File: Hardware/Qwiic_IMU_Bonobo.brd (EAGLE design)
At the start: 30.5 x 25.4 mm, 33 parts, among them J2 SMD, J3 PTH, J4 SMD, J6 SPI, U2 BNO080

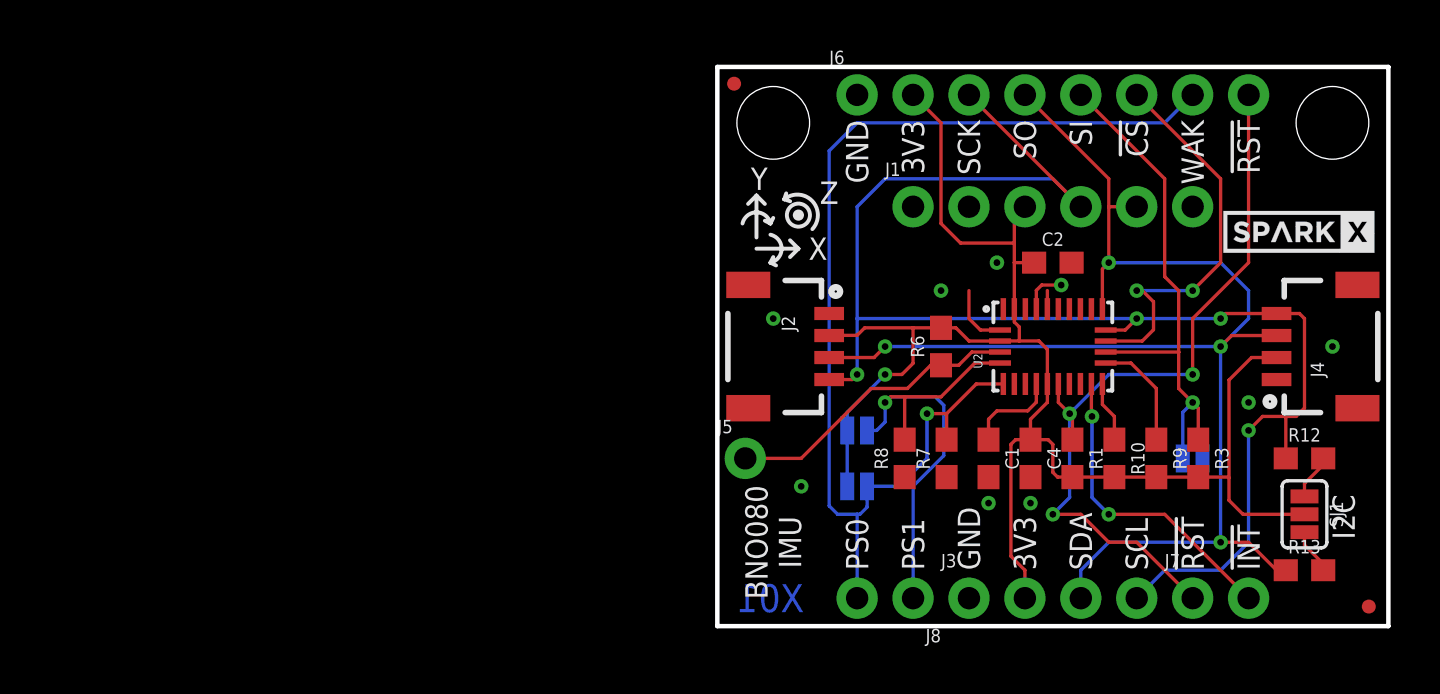
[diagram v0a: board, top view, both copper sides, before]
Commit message: Adding 32kHz xtal. Fixing UART silk.
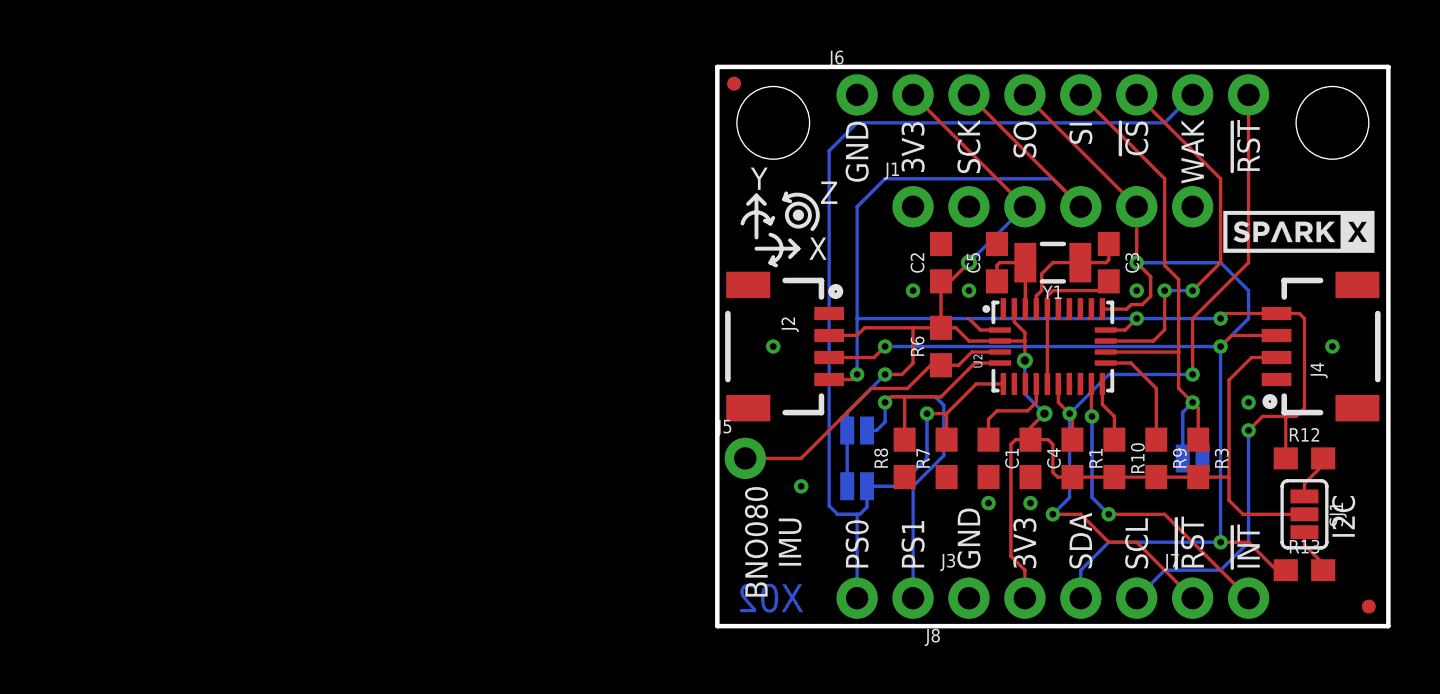
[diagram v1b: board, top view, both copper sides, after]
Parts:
- added C3, C5: 22pF, SparkFun-Capacitors:0603
- added Y1: 32.768kHz, SparkFun-Clocks:CRYSTAL-SMD-3.2X1.5MM
- moved C2 5.08 mm to (10.2, 16.5), turned to 90 degrees
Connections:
- new net N$1: C5.1, U2.27, Y1.P$2
- new net N$2: C3.1, U2.26, Y1.P$1
- net 3.3V: no longer U2.10
- net GND: now also C3.2, C5.2, U2.10; no longer U2.26
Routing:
- net N$2: track 0.00 -> 5.74 mm
- net N$1: track 0.00 -> 4.18 mm
- net GND: track 5.82 -> 8.68 mm
- net 3.3V: track 71.6 -> 69.9 mm, vias 1 -> 4
- net !CS: track 18.2 -> 16.9 mm
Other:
- board text added: "X02"
- board text removed: "3V#"
- board text removed: "X01"

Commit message: Label update. PWR LED added. Logo change.
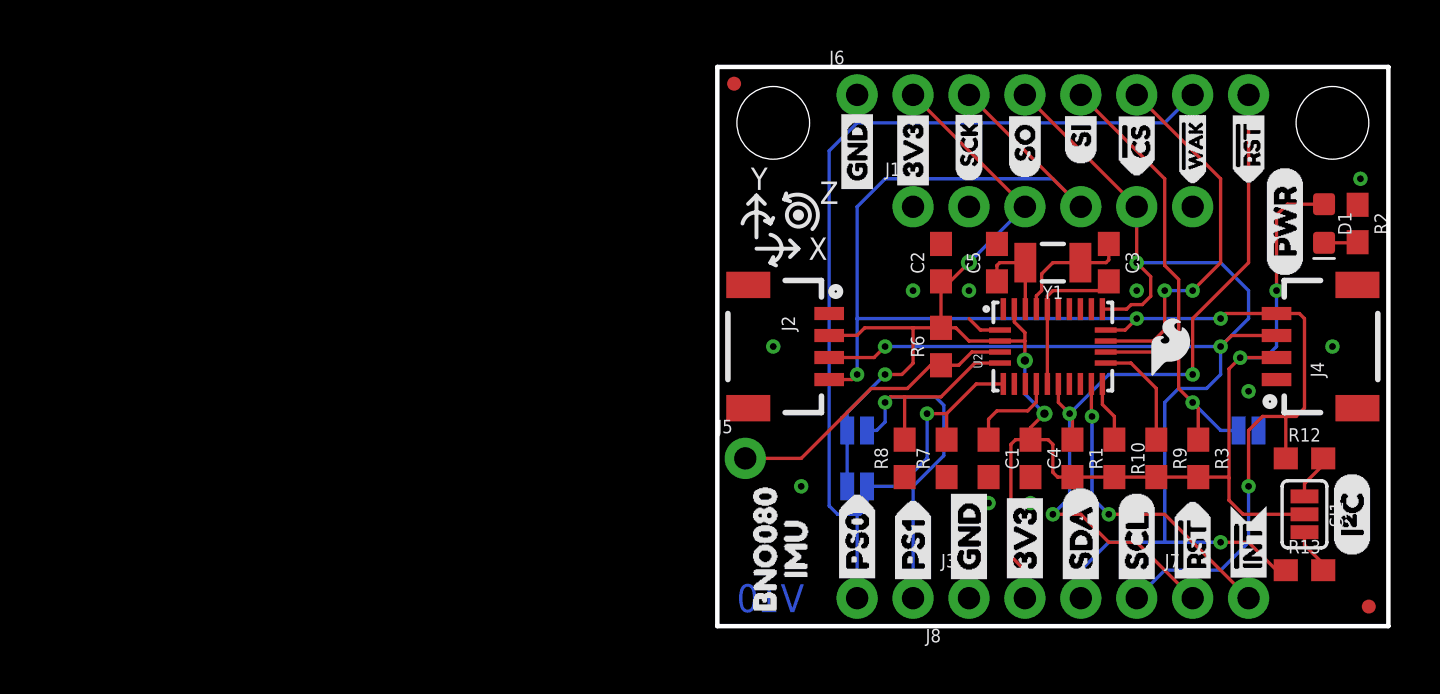
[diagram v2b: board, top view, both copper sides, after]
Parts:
- added D1: RED, SparkFun-LED:LED-0603
- added LOGO4: SFE_LOGO_FLAME.1_INCH, SparkFun-Aesthetics:SFE_LOGO_FLAME_.1
- added LOGO5: SFE_LOGO_NAME_FLAME.1_INCH, SparkFun-Aesthetics:SFE_LOGO_NAME_FLAME_.1
- added R2: 1k, SparkFun-Resistors:0603
- added U$10, U$9: (no value), Labels-0_04:3V3
- added U$11, U$50: (no value), buzzard_labels (4):3V30
- added U$12, U$13: (no value), buzzard_labels (6):SCK0
- added U$14: (no value), buzzard_labels (8):PS03
- added U$15, U$16: (no value), Labels-0_04:GND
- added U$17, U$18: (no value), buzzard_labels (7):SI1
- added U$19, U$20: (no value), buzzard_labels (5):#WAK6
- added U$21: (no value), buzzard_labels (8):3V32
- added U$22: (no value), buzzard_labels (8):RXI1
- added U$23: (no value), Labels-0_04:(I_SUPER2_C)
- added U$25, U$26: (no value), buzzard_labels (2):#INT0
- added U$27, U$28: (no value), buzzard_labels (2):PS14
- added U$29: (no value), buzzard_labels (2):PS05
- added U$3, U$4: (no value), Labels-0_04:#RST>
- added U$30: (no value), buzzard_labels (9):ADR0
- added U$33: (no value), buzzard_labels (2):PS114
- added U$34: (no value), buzzard_labels (2):PS015
- added U$35: (no value), buzzard_labels (8):TXO0
- added U$39: (no value), buzzard_labels (2):UART8
- added U$40: (no value), buzzard_labels (2):GRN10
- added U$41: (no value), buzzard_labels (2):BLK9
- added U$42, U$43: (no value), buzzard_labels (5):GND1
- added U$44: (no value), buzzard_labels (2):BNO080_IMU11
- added U$46: (no value), buzzard_labels (2):BNO08012
- added U$47: (no value), buzzard_labels (2):IMU13
- added U$49, U$51: (no value), buzzard_labels (5):#RST7
- added U$5, U$6: (no value), Labels-0_04:SCL
- added U$52, U$53: (no value), buzzard_labels (6):#CS3
- added U$54, U$55: (no value), buzzard_labels (7):SO0
- added U$7, U$8: (no value), Labels-0_04:SDA
- U$1: value SPARKX-LOGO3 -> (none); device SparkX:SPARKX-SMALL -> Labels-0_04:(PWR)
- U$2: value SPARKX-LOGO3 -> (none); device SparkX:SPARKX-SMALL -> buzzard_labels (11):BOOT2
- moved U$2 27.0 mm to (1.27, 8.00), flipped to the bottom, turned to 90 degrees
- moved U$1 12.0 mm to (25.8, 15.9), flipped to the top, turned to 90 degrees
- moved SJ2 2.84 mm to (24.1, 8.89)
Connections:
- new net N$3: D1.C, R2.2
- net 3.3V: now also D1.A
- net GND: now also R2.1
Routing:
- net 3.3V: track 69.9 -> 80.4 mm, vias 4 -> 6
- net SDA/MISO/TX: track 63.9 -> 65.7 mm
- net N$3: track 0.00 -> 1.54 mm
- net GND: vias 9 -> 10
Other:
- board text added: "V10"
- board text removed: "!CS"
- board text removed: "!INT"
- board text removed: "!RST"
- board text removed: "3V3"
- board text removed: "BLK"
- board text removed: "BNO080 IMU"
- board text removed: "GND"
- board text removed: "GRN"
- board text removed: "I2C"
- board text removed: "I2C ADR"
- board text removed: "PS0"
- board text removed: "PS1"
- board text removed: "RXI"
- board text removed: "SCK"
- board text removed: "SCL"
- board text removed: "SDA"
- board text removed: "SI"
- board text removed: "SO"
- board text removed: "TXO"
- board text removed: "UART"
- board text removed: "WAK"
- board text removed: "X02"

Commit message: Adding dims.
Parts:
- moved U$2 0.13 mm to (1.27, 8.13)

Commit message: Adding fancy Qwiic logo.
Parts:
- added U$24: (no value), Qwiic#Label#png:QWIIC#LABEL#PNG

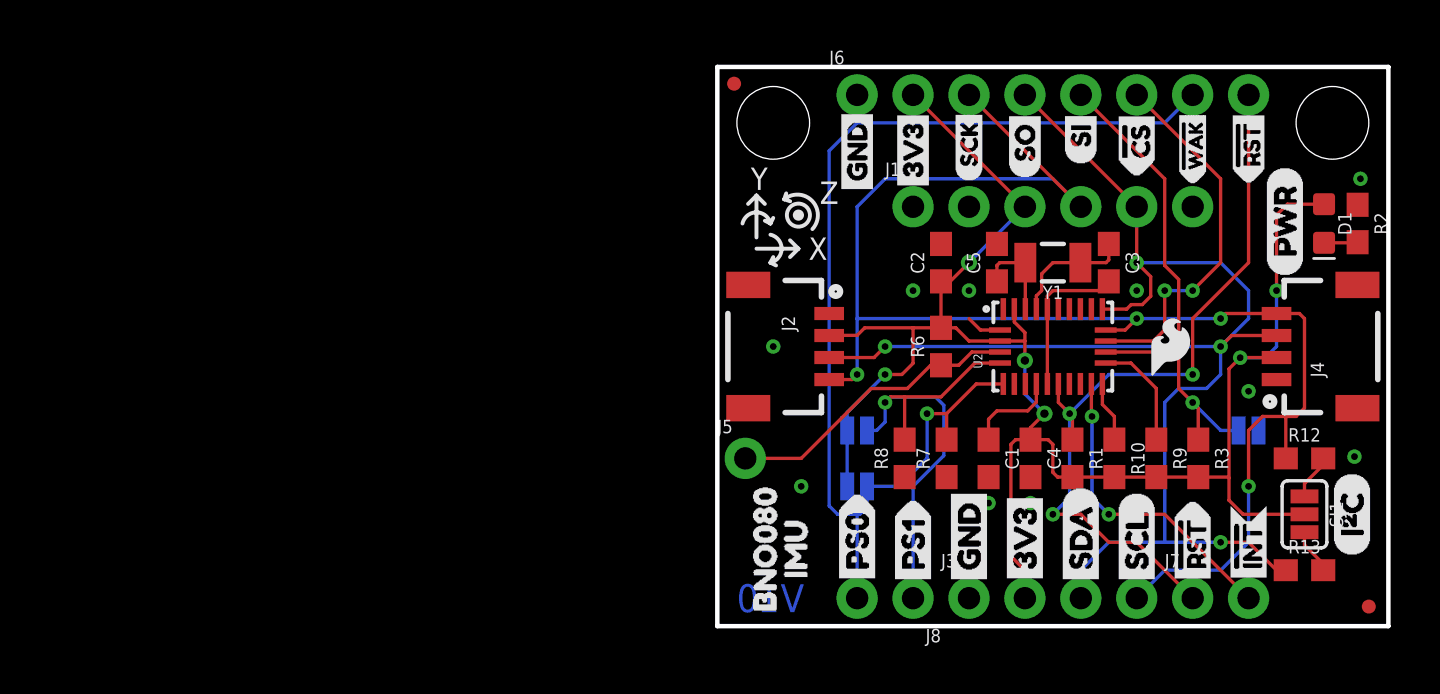
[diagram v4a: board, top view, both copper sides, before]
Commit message: Changing Qwiic logo to w/ word
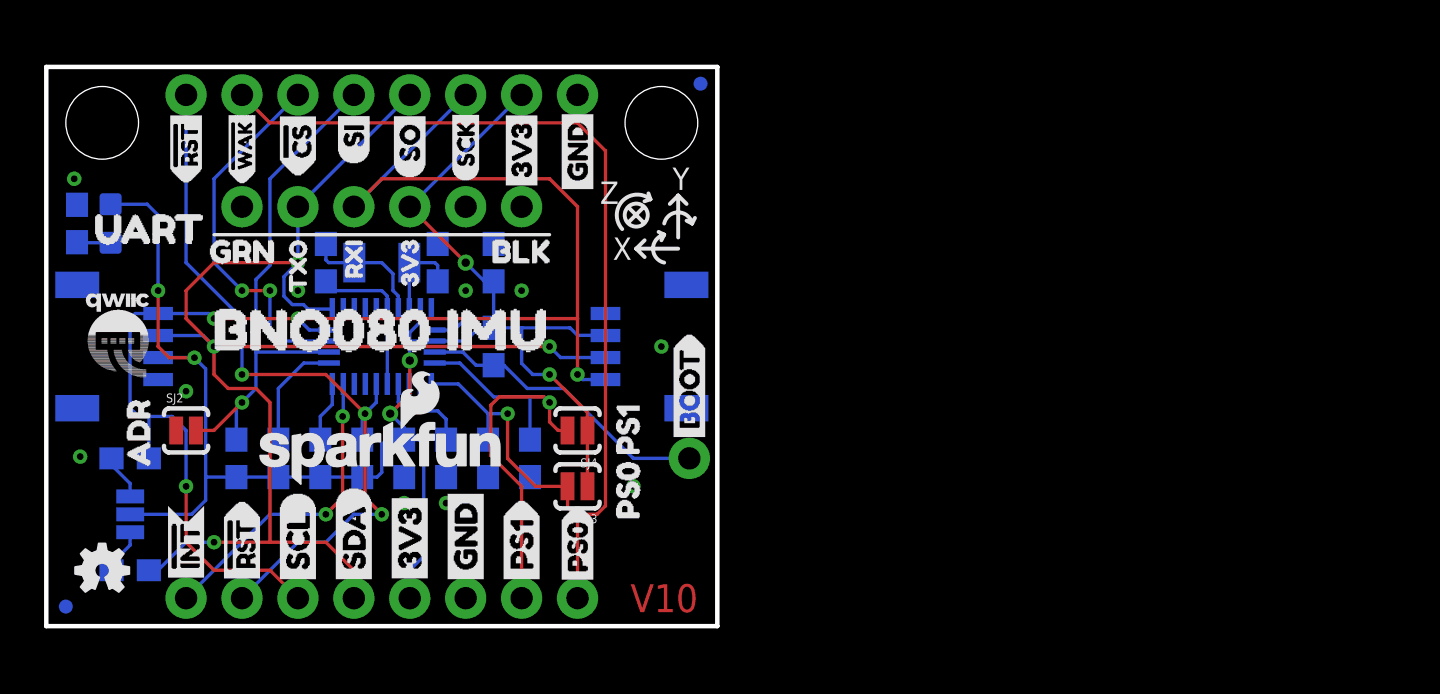
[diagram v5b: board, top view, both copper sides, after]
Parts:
- removed U$24: (no value), Qwiic#Label#png:QWIIC#LABEL#PNG
- added U$59: (no value), Qwiic#Label#Full#M#png (6):QWIIC#LABEL#FULL#M#PNG
- moved JP2 59.2 mm to (-29.6, 0.89), flipped to the bottom
- moved U$39 58.9 mm to (-29.5, 18.0), flipped to the top
- moved R2 58.2 mm to (-29.1, 18.3), flipped to the bottom
- moved U$23 57.7 mm to (-28.8, 3.17), flipped to the bottom
- moved JP4 55.9 mm to (-27.9, 22.9), flipped to the bottom
- moved LOGO1 55.9 mm to (-27.9, 2.54), flipped to the top
- moved D1 55.1 mm to (-27.6, 18.3), flipped to the bottom
- moved R12 53.3 mm to (-26.7, 7.62), flipped to the bottom
- moved R13 53.3 mm to (-26.7, 2.54), flipped to the bottom
- moved SJ1 53.3 mm to (-26.7, 5.08), flipped to the bottom
- moved U$30 52.6 mm to (-26.3, 6.35), flipped to the top
- moved U$1 51.6 mm to (-25.8, 15.9), flipped to the bottom
- moved J4 50.8 mm to (-25.4, 12.7), flipped to the bottom
- moved U$44 49.0 mm to (-24.5, 13.5), flipped to the top
- moved SJ2 48.3 mm to (-24.1, 8.89), flipped to the top
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
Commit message: Adding qwiic logo w/ words
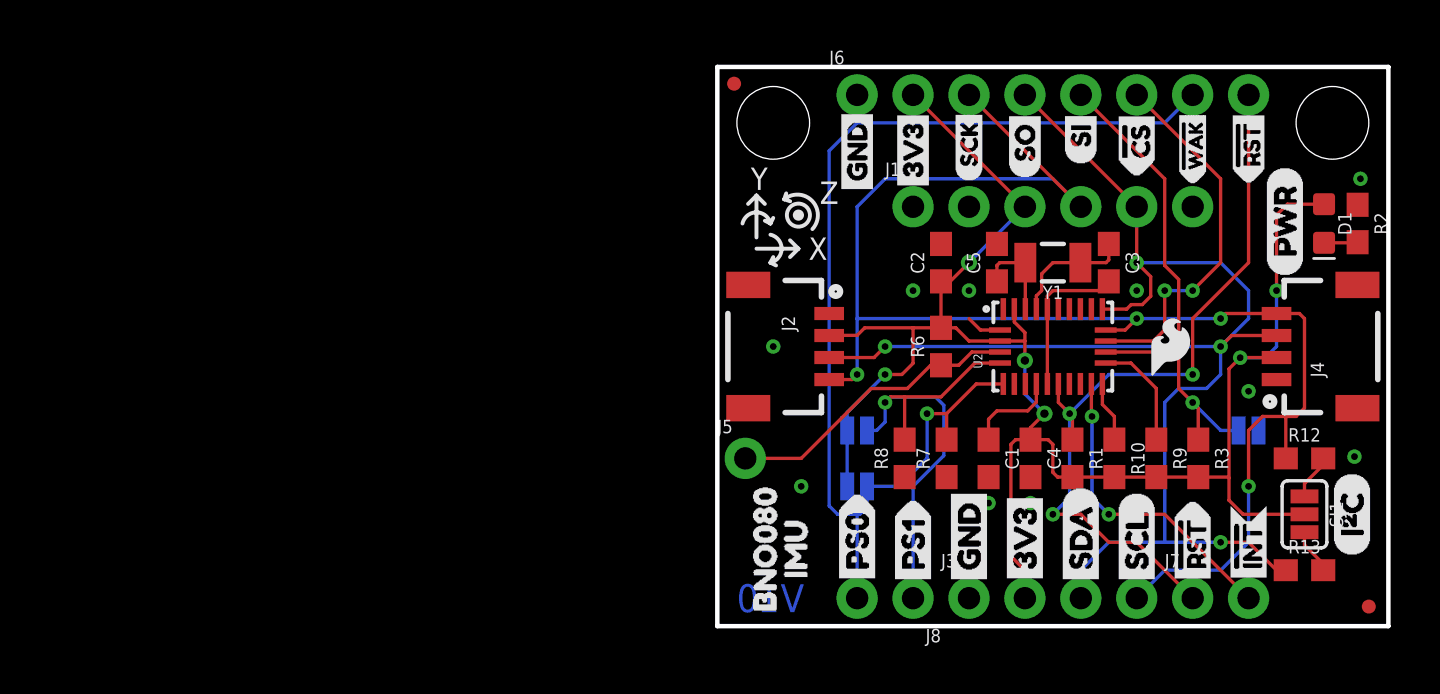
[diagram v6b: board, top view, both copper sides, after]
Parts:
- moved JP2 59.2 mm to (29.6, 0.89), flipped to the top
- moved U$39 58.9 mm to (29.5, 18.0), flipped to the bottom
- moved R2 58.2 mm to (29.1, 18.3), flipped to the top
- moved U$23 57.7 mm to (28.8, 3.17), flipped to the top
- moved JP4 55.9 mm to (27.9, 22.9), flipped to the top
- moved LOGO1 55.9 mm to (27.9, 2.54), flipped to the bottom
- moved D1 55.1 mm to (27.6, 18.3), flipped to the top
- moved U$59 54.6 mm to (27.3, 13.2), flipped to the bottom
- moved R12 53.3 mm to (26.7, 7.62), flipped to the top
- moved R13 53.3 mm to (26.7, 2.54), flipped to the top
- moved SJ1 53.3 mm to (26.7, 5.08), flipped to the top
- moved U$30 52.6 mm to (26.3, 6.35), flipped to the bottom
- moved U$1 51.6 mm to (25.8, 15.9), flipped to the top
- moved J4 50.8 mm to (25.4, 12.7), flipped to the top
- moved U$44 49.0 mm to (24.5, 13.5), flipped to the bottom
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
